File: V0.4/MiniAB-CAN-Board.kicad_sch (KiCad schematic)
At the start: 134 parts, among them J1 PC-FAN, J10 USB_B_Micro, J11 CAN, J12 ENDSTOP1, J13 ENDSTOP2, J14 PROBE, J2 PC-FAN, J3 HE-FAN, J4 TH0, J5 I2C, J6 H0, J7 NEOPIXEL, J8 STEPPER, J9 Conn_02x03_Top_Bottom, Q1 AO3400A, Q2 AO3400A, Q3 AON7418, U1 ADXL345BCCZ-RL7, U2 STM32F103C8Tx, U3 74LVC1G17, U4 LP5907MFX-3.3, U5 TMC2209-LA, U6 TPS56339DDC, U7 TPS54202DDC, U8 TCAN330, Y1 8MHz

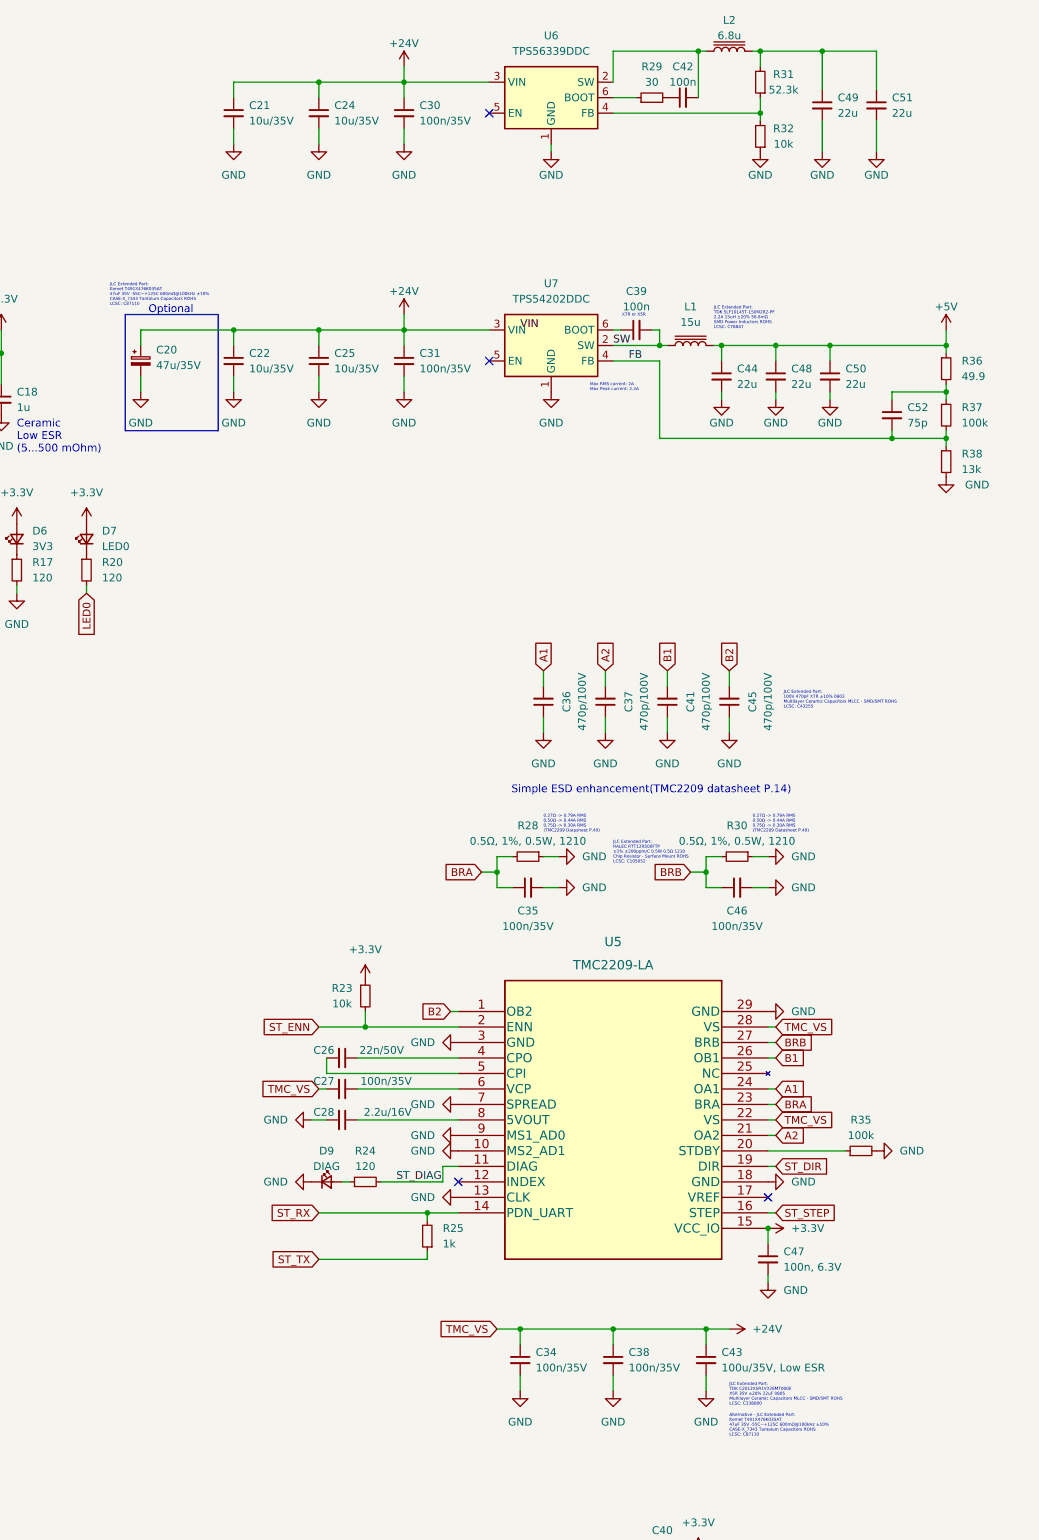
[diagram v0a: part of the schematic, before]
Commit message: Add THT JST version with new DCDC converter
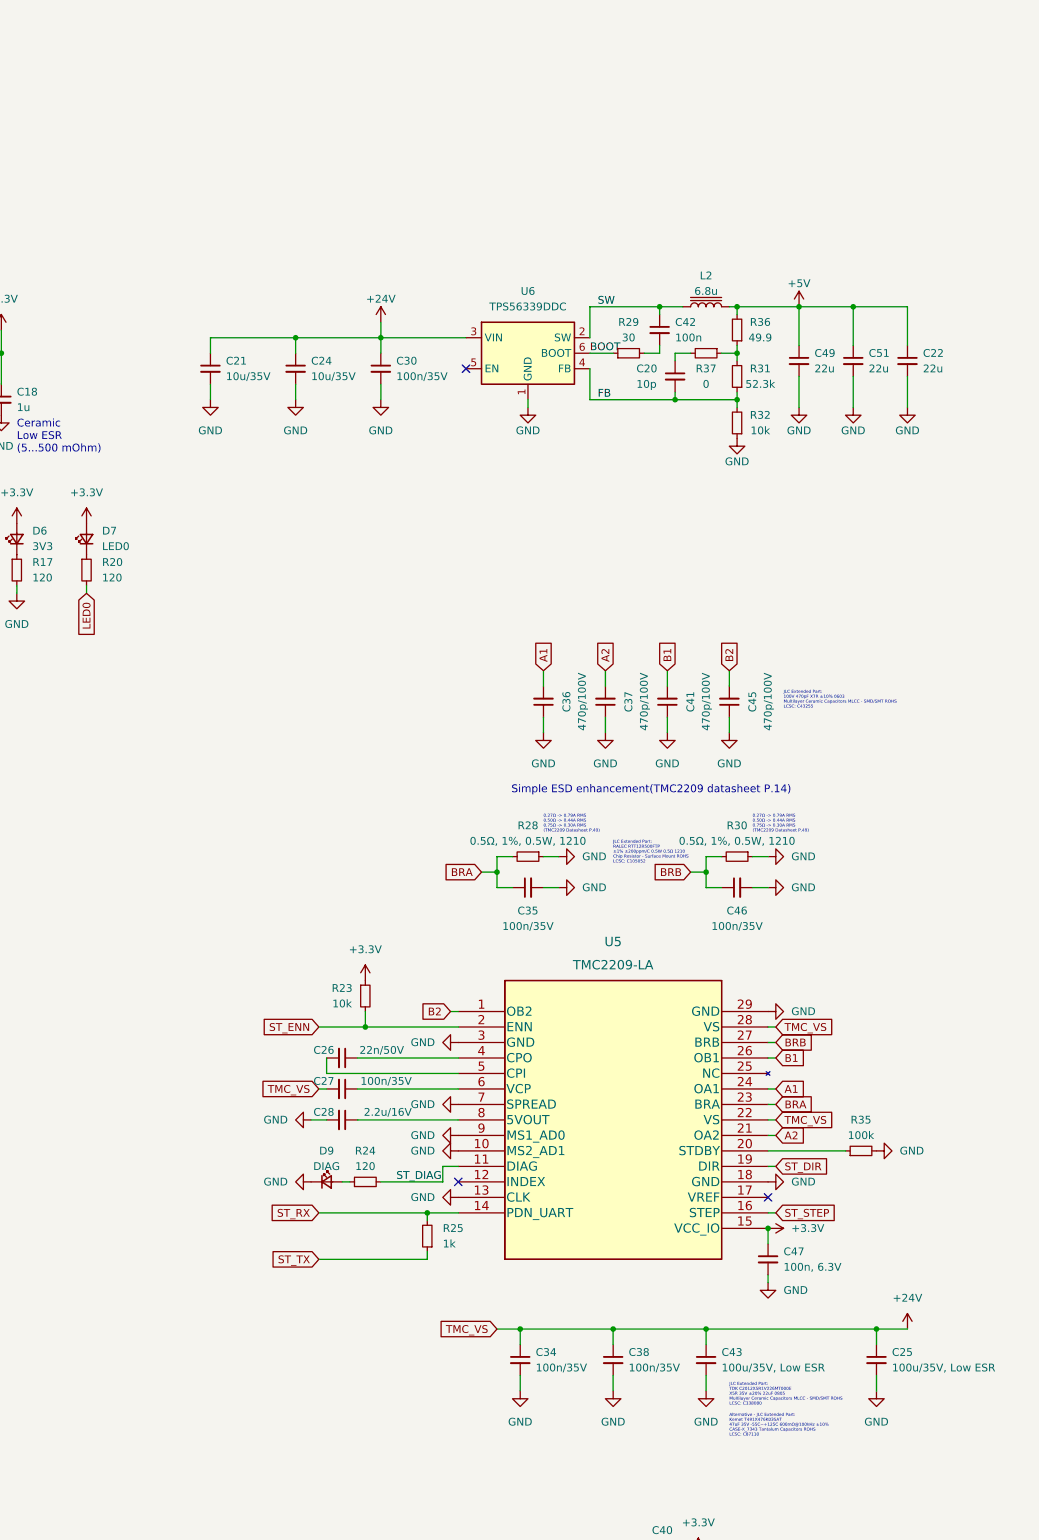
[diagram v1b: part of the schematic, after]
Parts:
- removed C20: 47u/35V, Capacitor_Tantalum_SMD:CP_EIA-7343-43_Kemet-X, symbol Device:C_Polarized_Small
- removed C31: 100n/35V, Capacitor_SMD:C_0402_1005Metric, symbol Device:C_Small
- removed C39: 100n, Capacitor_SMD:C_0402_1005Metric, symbol Device:C_Small
- removed C44, C48, C50: 22u, Capacitor_SMD:C_0805_2012Metric, symbol Device:C_Small
- removed C52: 75p, Capacitor_SMD:C_0402_1005Metric, symbol Device:C_Small
- removed L1: 15u, Inductor_SMD:L_TDK_SLF10145, symbol Device:L_Iron
- removed R38: 13k, Resistor_SMD:R_0603_1608Metric, symbol Device:R_Small
- removed U7: TPS54202DDC, Package_TO_SOT_SMD:SOT-23-6, symbol Regulator_Switching:TPS54202DDC
- added C20: 10p, Capacitor_SMD:C_0402_1005Metric, symbol Device:C_Small
- C22: value 10u/35V -> 22u
- C25: value 10u/35V -> 100u/35V, Low ESR
- J12, J13, J14, J7: footprint Connector_JST:JST_PH_B3B-PH-SM4-TB_1x03-1MP_P2.00mm_Vertical -> Connector_JST:JST_PH_B3B-PH-K_1x03_P2.00mm_Vertical
- J3, J4: footprint Connector_JST:JST_PH_B2B-PH-SM4-TB_1x02-1MP_P2.00mm_Vertical -> Connector_JST:JST_PH_B2B-PH-K_1x02_P2.00mm_Vertical
- J5: footprint Connector_JST:JST_PH_B4B-PH-SM4-TB_1x04-1MP_P2.00mm_Vertical -> Connector_JST:JST_PH_B4B-PH-K_1x04_P2.00mm_Vertical
- J6: footprint Connector_Molex:Molex_Micro-Fit_3.0_43650-0200_1x02_P3.00mm_Horizontal -> Connector_Molex:Molex_Micro-Fit_3.0_43045-0200_2x01_P3.00mm_Horizontal
- R37: value 100k -> 0; footprint Resistor_SMD:R_0603_1608Metric -> Resistor_SMD:R_0402_1005Metric
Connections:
- net +24V: no longer C22.1
- net +5V: now also C22.1, C49.1, C51.1, L2.2, R36.2; no longer R36.1
- net FB: now also R31.1, R32.2, U6.4 (FB), C20.2; no longer R37.2
- net SW: now also C42.1, L2.1, U6.2 (SW)
- net at R37.1: now also R31.2, R36.1; no longer R36.2
- net BOOT: now reaches R29.1, U6.6 (BOOT)
- net at R29.2: now also C42.2; no longer C42.1
- new net: C20.1, R37.2
- no-connect marks 10 -> 9
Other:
- note removed: "JLC Extended Part: Kemet T491X476K035AT 47uF 35V -55C~+125C 600mΩ@100kHz ±10% CASE-X_7343 Tantalum Capacitors ROHS LCSC: C87110"
- note removed: "JLC Extended Part: TDK SLF10145T-150M2R2-PF 2.2A 15uH ±20% 56.6mΩ SMD Power Inductors ROHS LCSC: C76847"
- note removed: "Max RMS current: 2A Max Peak current: 2.2A"
- note removed: "Optional"
- note removed: "X7R or X5R"
- moved on the sheet: C21, C24, C30, C42, C49, C51, L2, R29, R31, R32, U6

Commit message: Update DCDC Section
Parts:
- R23: value 10k -> 100k
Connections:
- net ST_ENN: now also U2.2 (PC13); no longer U2.19 (PB1)
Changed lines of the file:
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@@
     )
   )
-  (global_label "ST_ENN" (shape input) (at 104.14 115.57 180) (fields_autoplaced)
+  (global_label "ST_ENN" (shape input) (at 104.14 102.87 180) (fields_autoplaced)
     (effects (font (size 1.27 1.27)) (justify right))
-    (property "Intersheet References" "${INTERSHEET_REFS}" (id 0) (at 94.7721 115.6494 0)
+    (property "Intersheet References" "${INTERSHEET_REFS}" (id 0) (at 94.7721 102.9494 0)
       (effects (font (size 1.27 1.27)) (justify right) hide)
     )
@@
     (in_bom yes) (on_board yes)
     (property "Reference" "R23" (id 0) (at 307.34 132.08 0))
-    (property "Value" "10k" (id 1) (at 307.34 134.62 0))
+    (property "Value" "100k" (id 1) (at 307.34 134.62 0))
     (property "Footprint" "Resistor_SMD:R_0402_1005Metric" (id 2) (at 311.15 133.35 0)
       (effects (font (size 1.27 1.27)) hide)
@@
     )
     (path "/e72113a4-fe04-4086-88c1-d8a9726b0867"
-      (reference "R23") (unit 1) (value "10k") (footprint "Resistor_SMD:R_0402_1005Metric")
+      (reference "R23") (unit 1) (value "100k") (footprint "Resistor_SMD:R_0402_1005Metric")
     )
     (path "/a90e5223-0bf9-48da-9aa2-4e0f146e36b2"

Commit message: V0.4 finished
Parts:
- added TP2: 3V3, TestPoint:TestPoint_Pad_D1.0mm, symbol Connector:TestPoint
- added TP3: 24V, TestPoint:TestPoint_Pad_D1.0mm, symbol Connector:TestPoint
- added TP4: GND, TestPoint:TestPoint_Pad_D1.0mm, symbol Connector:TestPoint
- J1, J2: value PC-FAN -> PCF
- J3: value HE-FAN -> HEF
- J9: value Conn_02x03_Top_Bottom -> DEBUG
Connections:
- net +24V: now also TP3.1
- net +3V3: now also J12.1 (Pin_1), J13.1 (Pin_1), J14.1 (Pin_1), TP2.1
- net +5V: no longer J12.1 (Pin_1), J13.1 (Pin_1), J14.1 (Pin_1)
- net ENDSTOP1: now also U2.28 (PB15); no longer U2.40 (PB4)
- net ENDSTOP2: now also U2.26 (PB13); no longer U2.41 (PB5)
- net GND: now also TP4.1
- net HE-FAN: now also U2.18 (PB0); no longer U2.26 (PB13)
- net HEATER: now also U2.41 (PB5); no longer U2.27 (PB14)
- net LED0: now also U2.11 (PA1)
- net NEOPIXEL: now also U2.31 (PA10); no longer U2.18 (PB0)
- net PROBE: now also U2.30 (PA9); no longer U2.39 (PB3)
- net ST_DIR: now also U2.39 (PB3); no longer U2.29 (PA8)
- net ST_RX: now also U2.43 (PB7); no longer U2.31 (PA10)
- net ST_STEP: now also U2.40 (PB4); no longer U2.28 (PB15)
- net ST_TX: now also U2.42 (PB6); no longer U2.30 (PA9)
- net TH0: now also U2.19 (PB1); no longer U2.12 (PA2)
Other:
- note removed: "Do not populate Optional addon"
- moved on the sheet: C17, C19, C23, J11, J12, J13, J14, J5, J7, J8, J9, R14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

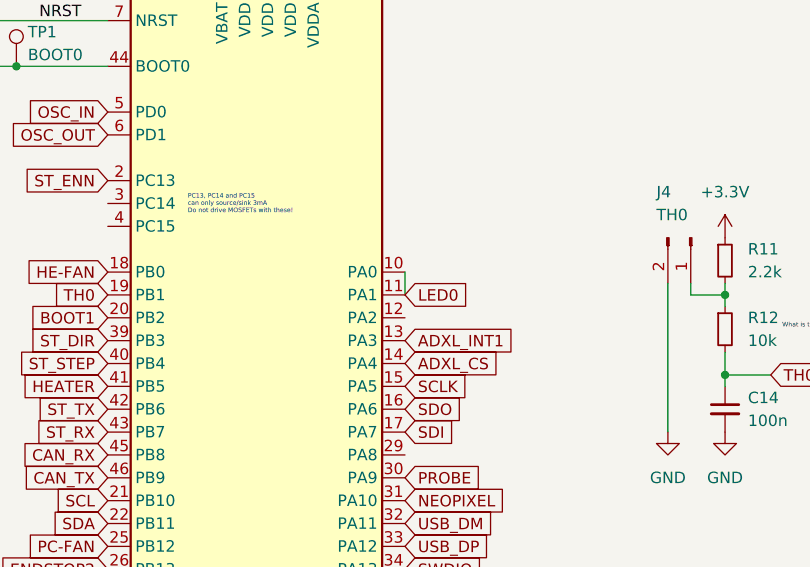
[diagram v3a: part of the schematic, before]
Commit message: Fix GND connection on TCAN330
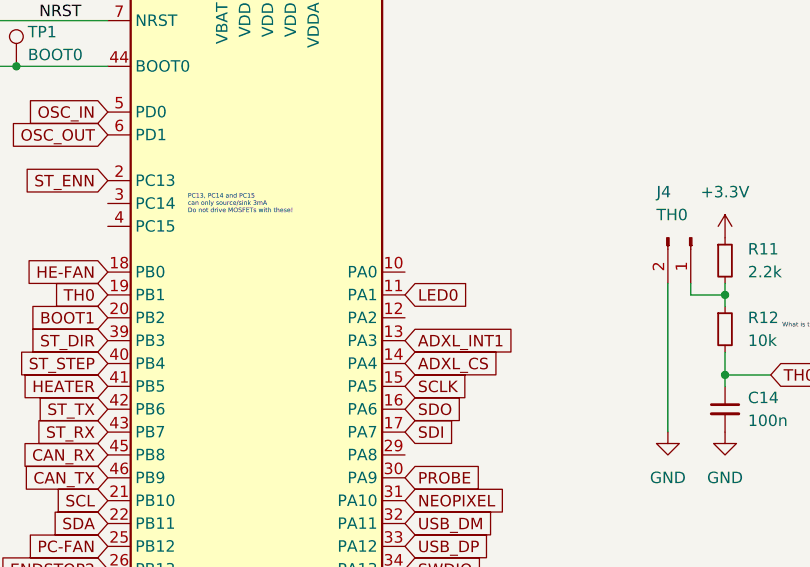
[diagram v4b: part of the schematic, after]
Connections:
- net LED0: no longer U2.10 (PA0)
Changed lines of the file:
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@@
-    (stroke (width 0) (type default) (color 0 0 0 0))
-  )
-  (wire (pts (xy 137.16 115.57) (xy 137.16 113.03))
     (stroke (width 0) (type default) (color 0 0 0 0))
   )

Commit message: Add silkscreen annotations
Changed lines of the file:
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@@
   (symbol (lib_id "74xGxx:74LVC1G17") (at 137.16 262.89 270) (unit 1)
     (in_bom yes) (on_board yes)
-    (property "Reference" "U3" (id 0) (at 144.78 255.27 0))
-    (property "Value" "74LVC1G17" (id 1) (at 142.24 255.27 0))
+    (property "Reference" "U3" (id 0) (at 142.24 256.54 90))
+    (property "Value" "74LVC1G17" (id 1) (at 146.05 259.08 90))
     (property "Footprint" "Package_TO_SOT_SMD:SOT-23-5" (id 2) (at 137.16 262.89 0)
       (effects (font (size 1.27 1.27)) hide)

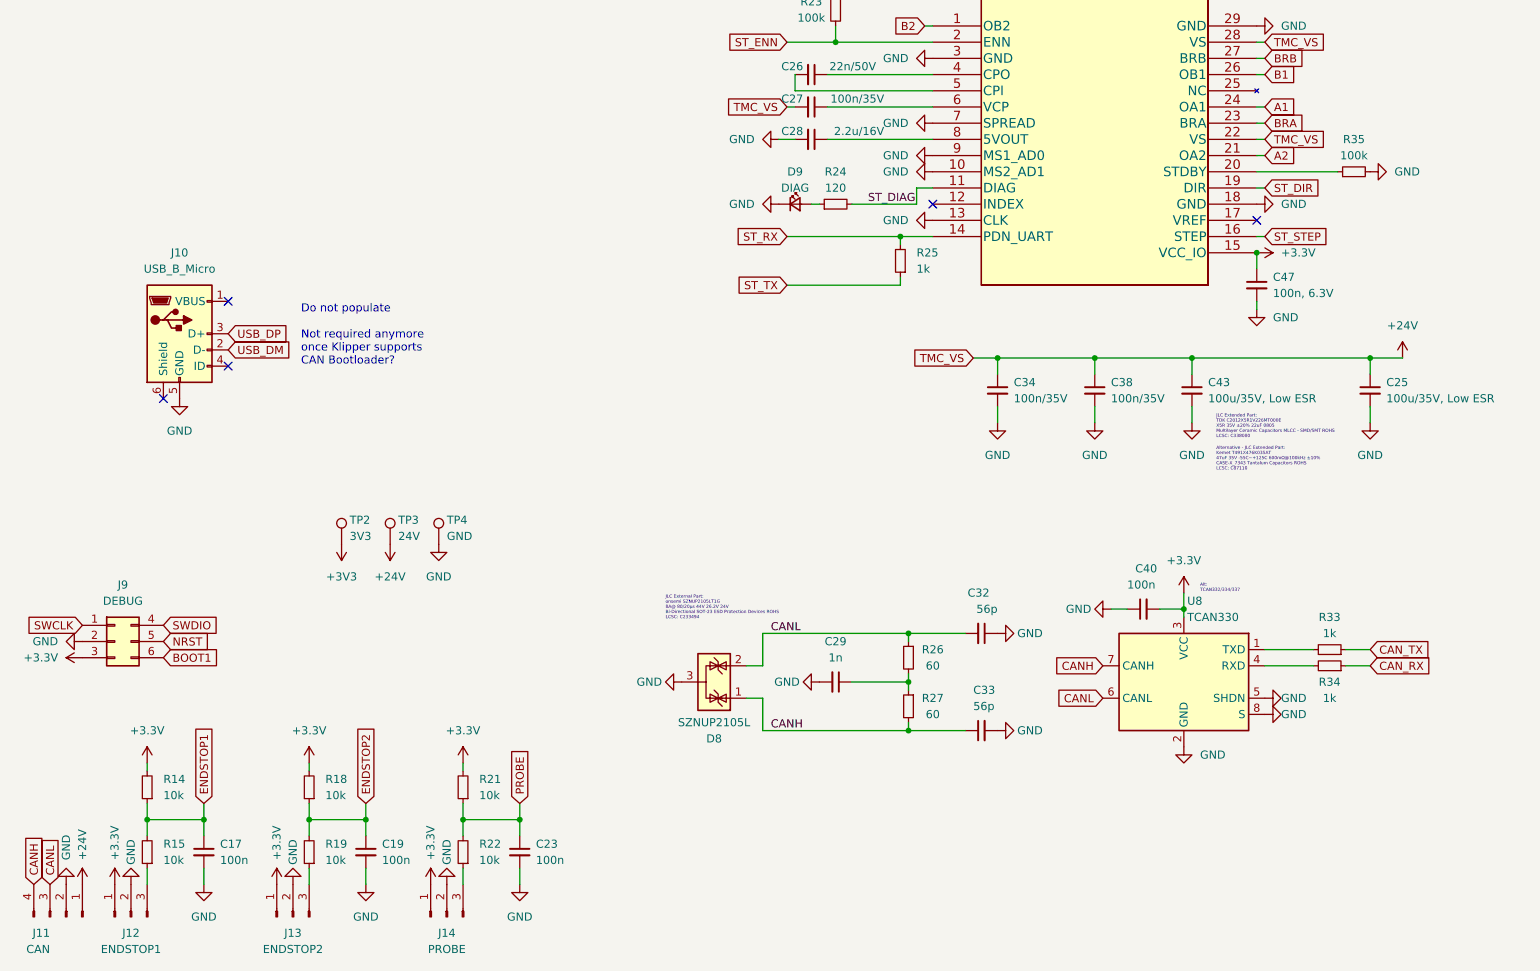
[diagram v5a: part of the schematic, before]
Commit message: Fix minor issues on schematic, pcb still pending
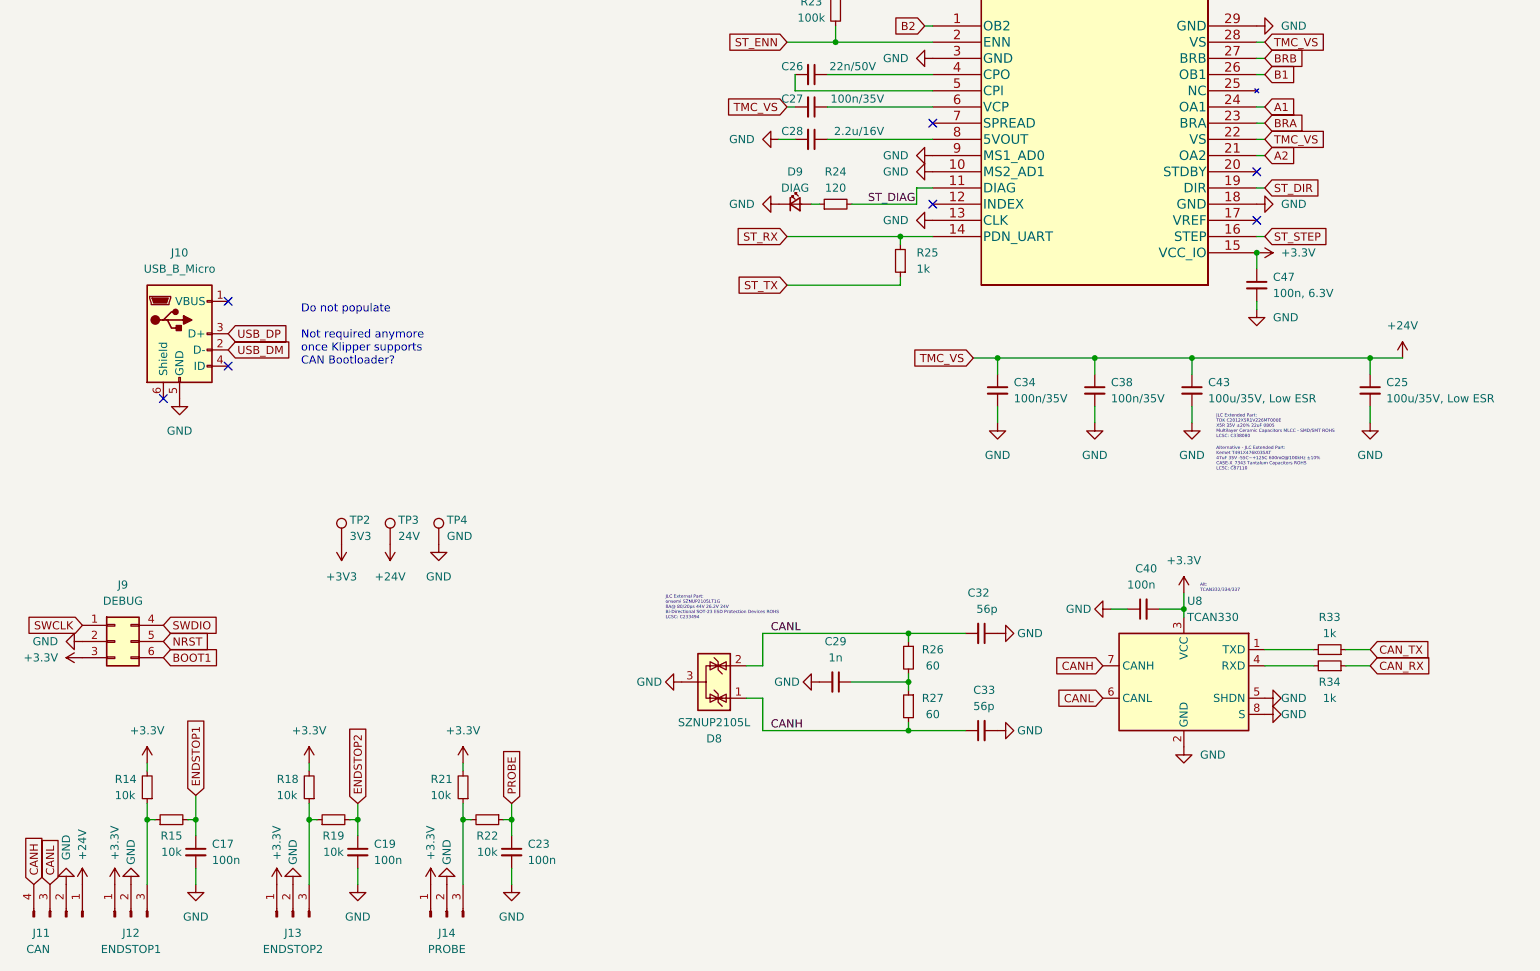
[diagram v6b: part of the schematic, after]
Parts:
- removed R35: 100k, Resistor_SMD:R_0402_1005Metric, symbol Device:R_Small
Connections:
- net ENDSTOP1: no longer R14.1
- net ENDSTOP2: no longer R18.1
- net GND: no longer U5.7 (SPREAD)
- net PROBE: now also R22.1; no longer R21.1, R22.2
- net at J14.3 (Pin_3): now also R21.1, R22.2; no longer R22.1
- net at J12.3 (Pin_3), R15.1: now also R14.1
- net at J13.3 (Pin_3), R19.1: now also R18.1
- no-connect marks 9 -> 11
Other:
- moved on the sheet: C17, C19, C23, R15, R19, R22
